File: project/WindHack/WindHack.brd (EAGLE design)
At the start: 79 x 43.7 mm, 48 parts, among them SW1 SSSS810701, SW2 SSSS810701, U1 LazuriteBLE, U10 BK-913, U2 BM1383AGLV, U3 KXG03, U4 BM1422AGMV, U5 DF40C-20DS-0.4V, U6 BHXXPB1WFV, U7 MOLEX-SD-503398-1892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

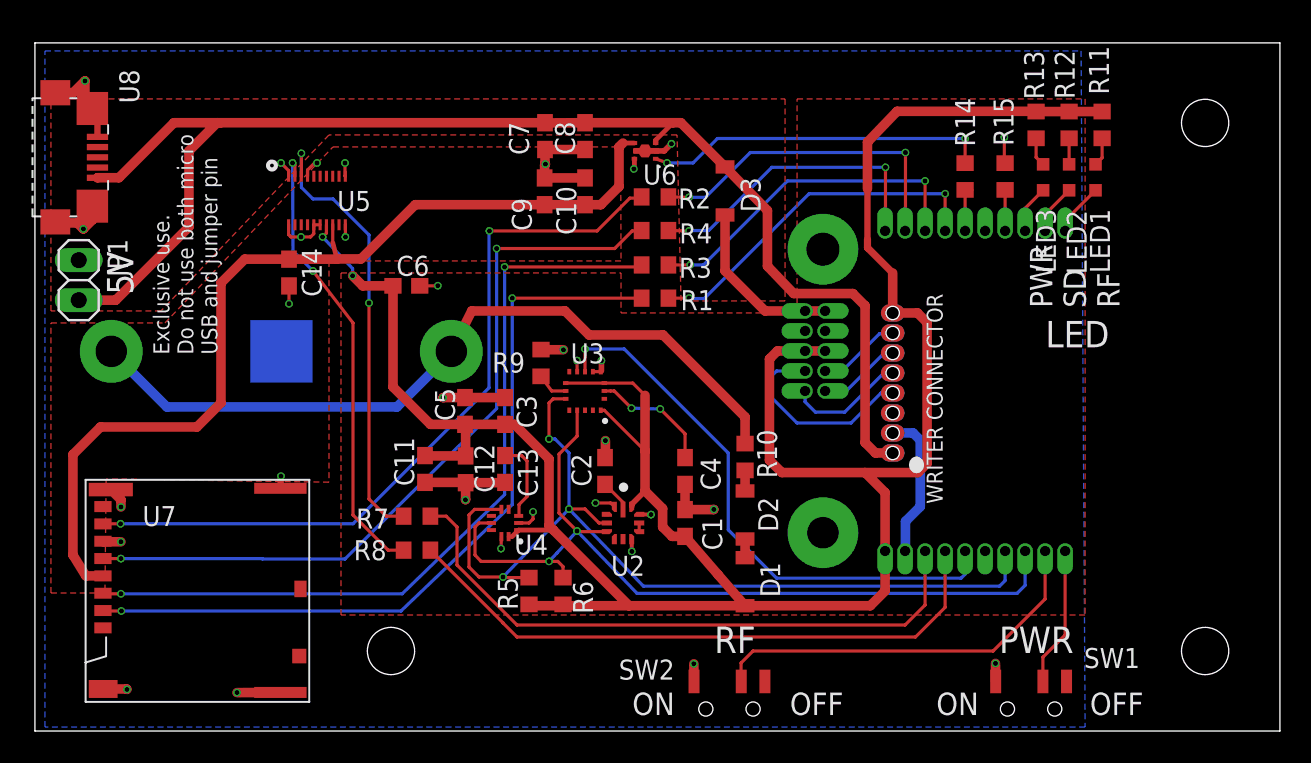
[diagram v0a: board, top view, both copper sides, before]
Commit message: modified to rev1A
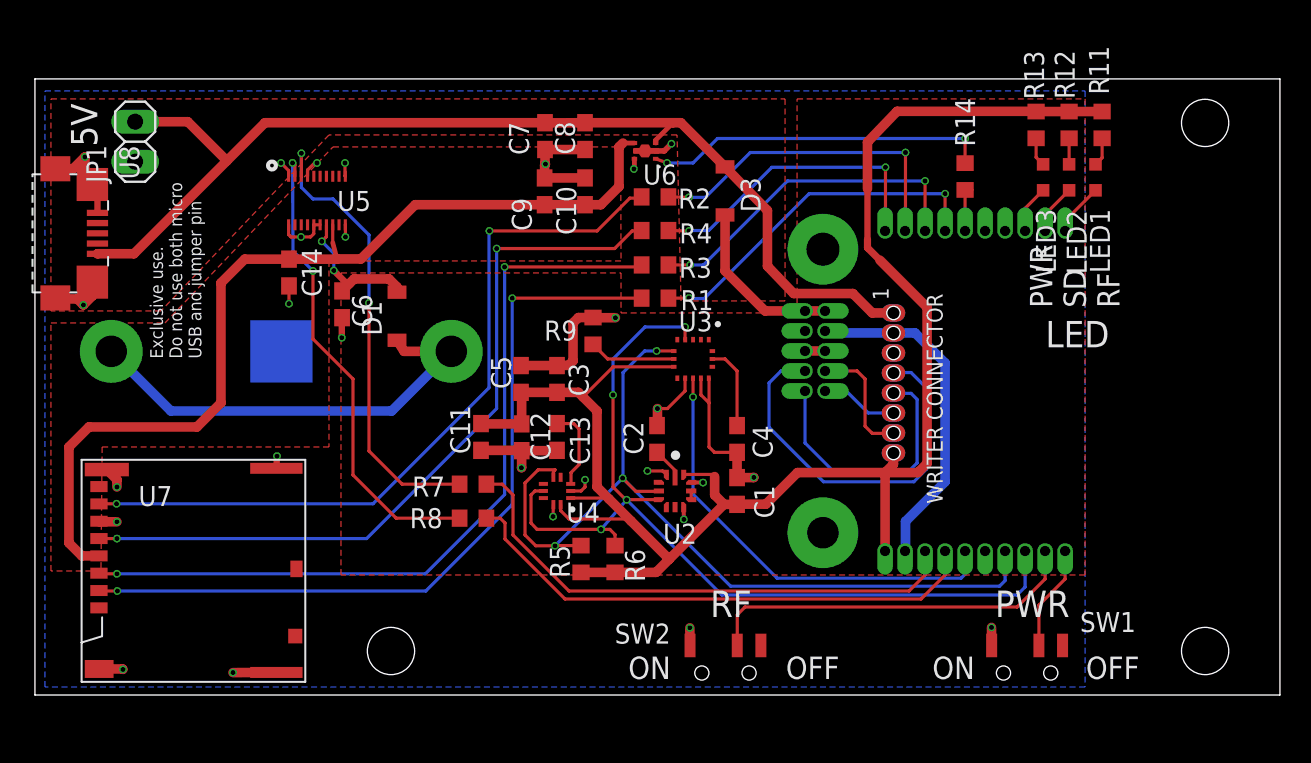
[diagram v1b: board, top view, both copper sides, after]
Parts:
- removed D2: RF071MM2S, lz-shield:RF071MM2S
- removed R10: 100, rcl:R0603
- removed R15: 0, rcl:R0603
- C6: value 0.1uF -> 1uF
- moved D1 27.8 mm to (35.1, 28.9), turned to 0 degrees
- moved JP1 9.49 mm to (18.4, 40.0), turned to 90 degrees
- moved U3 7.15 mm to (53.8, 26.2)
- moved U8 4.83 mm to (13.4, 34.1)
- moved C6 4.24 mm to (31.6, 29.6), turned to 270 degrees
- moved C11 4.10 mm to (40.4, 21.2)
- moved C12 4.10 mm to (43.0, 21.2)
- moved C5 4.10 mm to (42.9, 24.9)
- moved R8 4.10 mm to (39.9, 16.1)
- moved R7 4.10 mm to (39.9, 18.2)
- moved U4 3.88 mm to (45.2, 17.8)
- moved C13 3.88 mm to (45.2, 21.2)
- moved C3 3.88 mm to (45.2, 24.9)
- moved C1 3.88 mm to (56.6, 17.8)
- moved U2 3.88 mm to (52.7, 17.8)
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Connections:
- net ACCEL_INT renamed GYRO_INT
- net BT_SW renamed RF_SW
- removed net +2.4V_RSV: R10.2, U10.VDD1, U10.VDD2
- removed net GPS_PRS: R15.2, U1.7
- removed net N$9: D2.C, R10.1
- new net +3V_RSV: C6.1, D1.A, U5.14
- net +3V3: no longer C6.1, D1.A, U5.14
- net GND: no longer R15.1
- net N$8: now also U10.VDD1, U10.VDD2; no longer D2.A
- net TEST0: now also U$1.7_1; no longer U$1.7_2
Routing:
- net +3V3: track 161.7 -> 110.8 mm, vias 2 -> 0
- net +2.4V_RSV: track 49.4 -> 0.00 mm
- net N$8: track 1.19 -> 28.6 mm
- net GND: track 72.6 -> 94.6 mm, vias 32 -> 28
- net +5V: track 85.9 -> 69.7 mm
- net TEST1N: track 12.8 -> 24.9 mm
- net 1: track 7.55 -> 17.1 mm
- net +3V_RSV: track 0.00 -> 9.03 mm, vias 0 -> 2
- net GYRO_INT: track 36.0 -> 28.4 mm
- net SERIAL2_RX: track 39.6 -> 34.1 mm
- net SERIAL2_TX: track 39.4 -> 34.1 mm
- net SCL: track 55.2 -> 59.4 mm, vias 2 -> 4
- net N$5: track 2.04 -> 5.51 mm
- net GPS_PRS: track 2.60 -> 0.00 mm
- net TEST0: track 5.29 -> 7.75 mm
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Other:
- board size 79 x 43.7 mm -> 79 x 39.1 mm
- board text added: "1"
- board text added: "WindHack rev1A"
- board text removed: "WindHack rev1"
- board text removed: "●"

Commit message: updated to rev 1A'
- moved C6/C4/D1 location
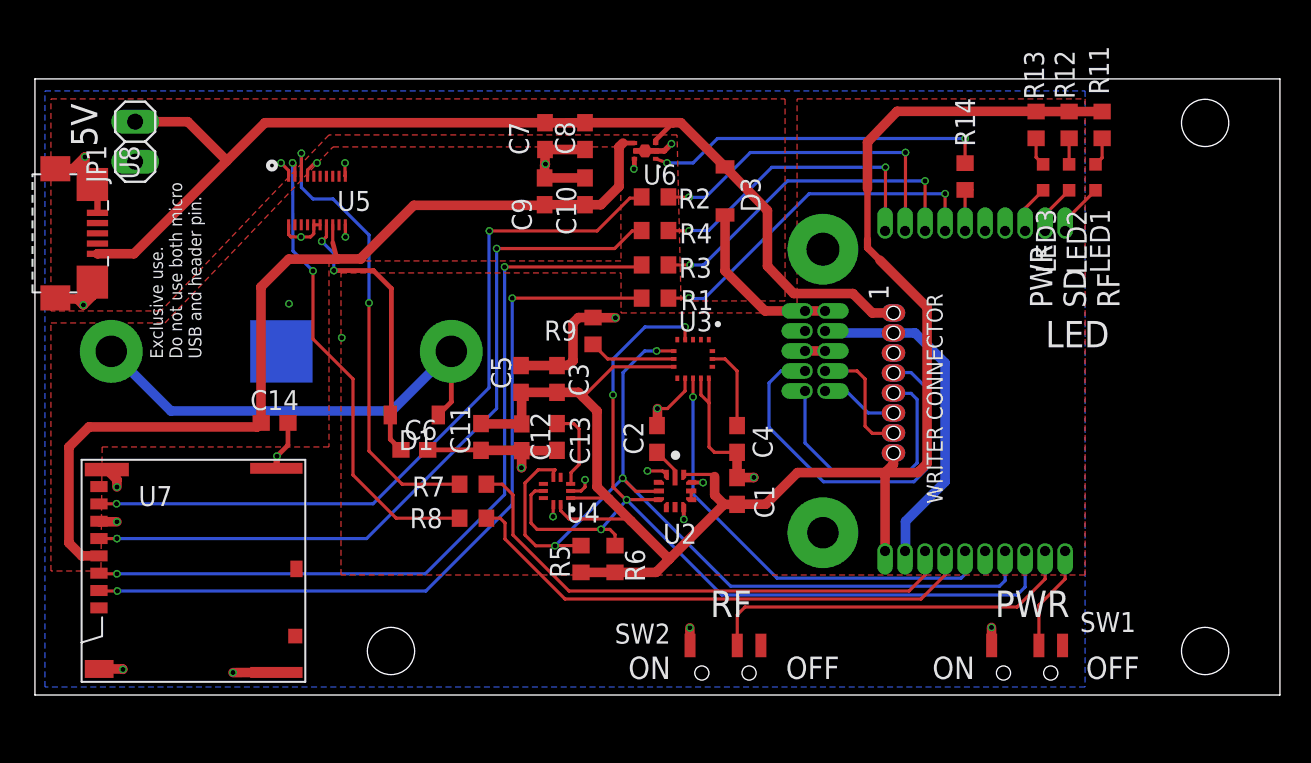
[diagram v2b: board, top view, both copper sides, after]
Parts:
- moved C6 10.3 mm to (36.2, 20.4), turned to 0 degrees
- moved C14 9.59 mm to (27.3, 22.1), turned to 0 degrees
- moved D1 6.36 mm to (36.1, 22.6), turned to 90 degrees
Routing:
- net +3V_RSV: track 9.03 -> 18.0 mm
- net GND: track 94.6 -> 98.0 mm
- net LDO3V: track 60.4 -> 61.0 mm
- net N$8: track 28.6 -> 29.1 mm
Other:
- board text added: "Exclusive use. Do not use both micro USB and header pin."
- board text removed: "Exclusive use. Do not use both micro USB and jumper pin"

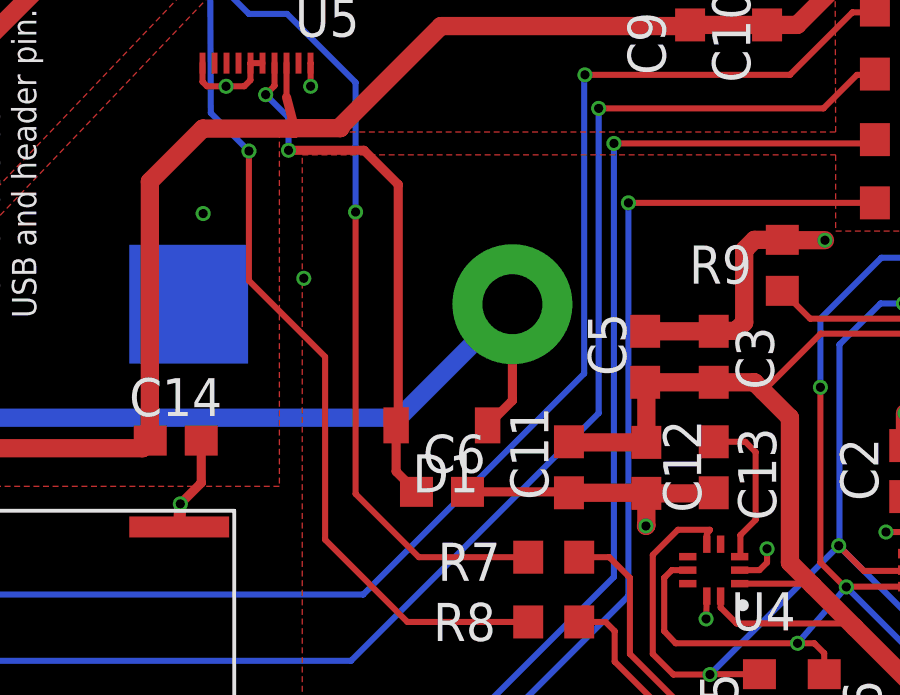
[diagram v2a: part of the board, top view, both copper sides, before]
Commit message: update WindHack and lz-shield(RF071MM2S)
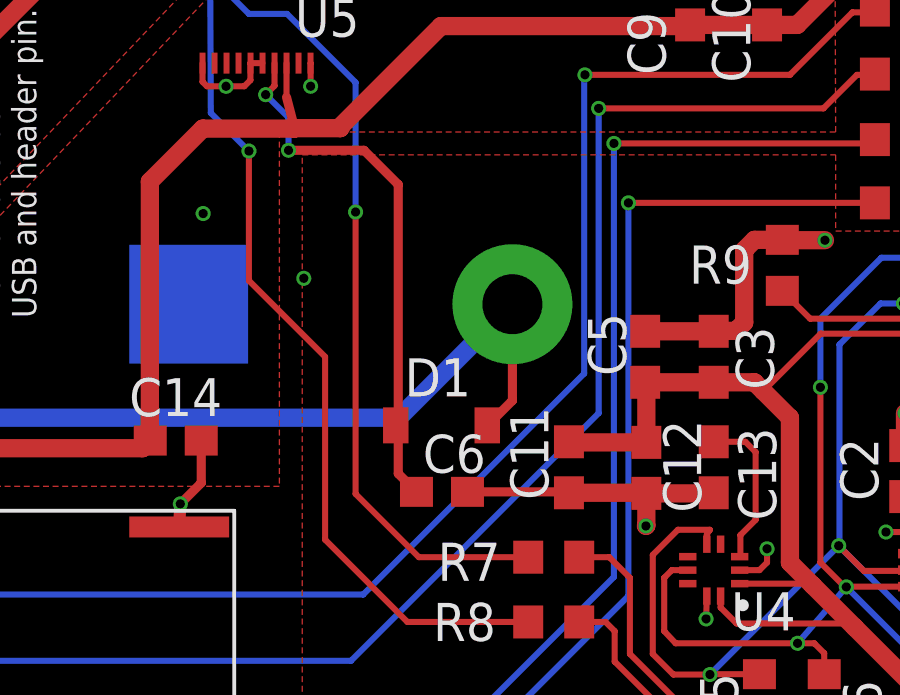
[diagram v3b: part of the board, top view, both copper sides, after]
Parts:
- turned D1 to 270 degrees
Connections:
- net +3V_RSV: now also D1.C; no longer D1.A
- net N$8: now also D1.A; no longer D1.C
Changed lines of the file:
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@@
 <layers>
 <layer number="1" name="Top" color="4" fill="1" visible="yes" active="yes"/>
-<layer number="16" name="Bottom" color="1" fill="1" visible="yes" active="yes"/>
+<layer number="16" name="Bottom" color="1" fill="1" visible="no" active="yes"/>
 <layer number="17" name="Pads" color="2" fill="1" visible="yes" active="yes"/>
 <layer number="18" name="Vias" color="2" fill="1" visible="yes" active="yes"/>
 <layer number="19" name="Unrouted" color="6" fill="1" visible="yes" active="yes"/>
 <layer number="20" name="Dimension" color="15" fill="1" visible="yes" active="yes"/>
-<layer number="21" name="tPlace" color="7" fill="1" visible="yes" active="yes"/>
-<layer number="22" name="bPlace" color="7" fill="1" visible="yes" active="yes"/>
+<layer number="21" name="tPlace" color="7" fill="1" visible="no" active="yes"/>
+<layer number="22" name="bPlace" color="7" fill="1" visible="no" active="yes"/>
 <layer number="23" name="tOrigins" color="15" fill="1" visible="no" active="yes"/>
 <layer number="24" name="bOrigins" color="15" fill="1" visible="no" active="yes"/>
-<layer number="25" name="tNames" color="7" fill="1" visible="no" active="yes"/>
+<layer number="25" name="tNames" color="7" fill="1" visible="yes" active="yes"/>
 <layer number="26" name="bNames" color="7" fill="1" visible="no" active="yes"/>
 <layer number="27" name="tValues" color="7" fill="1" visible="no" active="yes"/>
@@
 <layer number="37" name="tTest" color="7" fill="1" visible="no" active="yes"/>
 <layer number="38" name="bTest" color="7" fill="1" visible="no" active="yes"/>
-<layer number="39" name="tKeepout" color="4" fill="11" visible="no" active="yes"/>
+<layer number="39" name="tKeepout" color="4" fill="11" visible="yes" active="yes"/>
 <layer number="40" name="bKeepout" color="1" fill="11" visible="no" active="yes"/>
-<layer number="41" name="tRestrict" color="4" fill="10" visible="no" active="yes"/>
+<layer number="41" name="tRestrict" color="4" fill="10" visible="yes" active="yes"/>
 <layer number="42" name="bRestrict" color="1" fill="10" visible="no" active="yes"/>
 <layer number="43" name="vRestrict" color="2" fill="10" visible="no" active="yes"/>
-<layer number="44" name="Drills" color="7" fill="1" visible="no" active="yes"/>
-<layer number="45" name="Holes" color="7" fill="1" visible="no" active="yes"/>
+<layer number="44" name="Drills" color="7" fill="1" visible="yes" active="yes"/>
+<layer number="45" name="Holes" color="7" fill="1" visible="yes" active="yes"/>
 <layer number="46" name="Milling" color="3" fill="1" visible="no" active="yes"/>
-<layer number="47" name="Measures" color="7" fill="1" visible="no" active="yes"/>
+<layer number="47" name="Measures" color="7" fill="1" visible="yes" active="yes"/>
 <layer number="48" name="Document" color="7" fill="1" visible="yes" active="yes"/>
 <layer number="49" name="Reference" color="7" fill="1" visible="yes" active="yes"/>
 <layer number="50" name="dxf" color="7" fill="1" visible="no" active="no"/>
 <layer number="51" name="tDocu" color="7" fill="1" visible="yes" active="yes"/>
-<layer number="52" name="bDocu" color="7" fill="1" visible="yes" active="yes"/>
+<layer number="52" name="bDocu" color="7" fill="1" visible="no" active="yes"/>
 <layer number="53" name="tGND_GNDA" color="7" fill="9" visible="no" active="no"/>
 <layer number="54" name="bGND_GNDA" color="1" fill="9" visible="no" active="no"/>
@@
 <attribute name="VALUE" x="58.42" y="34.29" size="1.27" layer="27" rot="R90"/>
 </element>
-<element name="D1" library="lz-shield" package="RF071MM2S" value="RF071MM2S" x="36.15" y="22.606" smashed="yes" rot="R90">
-<attribute name="NAME" x="35.1732" y="20.3708" size="1.27" layer="25"/>
-<attribute name="VALUE" x="38.69" y="25.146" size="1.27" layer="27" rot="R180"/>
+<element name="D1" library="lz-shield" package="RF071MM2S" value="RF071MM2S" x="36.1384" y="22.606" smashed="yes" rot="R270">
+<attribute name="NAME" x="37.1152" y="24.8412" size="1.27" layer="25" rot="R180"/>
+<attribute name="VALUE" x="33.5984" y="20.066" size="1.27" layer="27"/>
 </element>
 <element name="U4" library="lz-shield" package="BM1422AGMV" value="BM1422AGMV" x="45.212" y="17.78" smashed="yes" rot="R270">
@@
 </signal>
 <signal name="+3V_RSV">
-<contactref element="D1" pad="A"/>
 <contactref element="U5" pad="14"/>
 <contactref element="C6" pad="1"/>
@@
 <wire x1="30.2768" y1="33.6296" x2="31.0388" y2="32.8676" width="0.2032" layer="16"/>
 <wire x1="31.0388" y1="32.8676" x2="31.0388" y2="31.7754" width="0.2032" layer="16"/>
-<wire x1="35.3036" y1="20.3898" x2="34.625" y2="21.0684" width="0.3048" layer="1"/>
-<wire x1="34.625" y1="21.0684" x2="34.625" y2="22.606" width="0.3048" layer="1"/>
 <wire x1="31.0388" y1="31.7754" x2="33.5534" y2="31.7754" width="0.3048" layer="1"/>
 <wire x1="33.5534" y1="31.7754" x2="34.6964" y2="30.6324" width="0.3048" layer="1"/>
-<wire x1="34.6964" y1="30.6324" x2="34.6964" y2="22.6774" width="0.3048" layer="1"/>
-<wire x1="34.6964" y1="22.6774" x2="34.625" y2="22.606" width="0.3048" layer="1"/>
+<wire x1="34.6964" y1="30.6324" x2="34.6964" y2="22.606" width="0.3048" layer="1"/>
+<wire x1="34.6964" y1="22.606" x2="34.6964" y2="20.997" width="0.3048" layer="1"/>
+<wire x1="34.6964" y1="20.997" x2="35.3036" y2="20.3898" width="0.3048" layer="1"/>
+<contactref element="D1" pad="C"/>
+<wire x1="34.6134" y1="22.606" x2="34.6964" y2="22.606" width="0.3048" layer="1"/>
 </signal>
 <signal name="RF_SW">
@@
 <contactref element="U10" pad="VDD2"/>
 <contactref element="U10" pad="VDD1"/>
-<contactref element="D1" pad="C"/>
 <wire x1="16.9114" y1="26.6446" x2="20.696" y2="22.86" width="0.6096" layer="16"/>
 <wire x1="20.696" y1="22.86" x2="34.7168" y2="22.86" width="0.6096" layer="16"/>
 <wire x1="38.5014" y1="26.6446" x2="34.7168" y2="22.86" width="0.6096" layer="16"/>
 <wire x1="38.5014" y1="26.6446" x2="38.5014" y2="23.4324" width="0.3048" layer="1"/>
-<wire x1="38.5014" y1="23.4324" x2="37.675" y2="22.606" width="0.3048" layer="1"/>
+<contactref element="D1" pad="A"/>
+<wire x1="37.6634" y1="22.606" x2="37.675" y2="22.606" width="0.2032" layer="1"/>
+<wire x1="37.675" y1="22.606" x2="38.5014" y2="23.4324" width="0.3048" layer="1"/>
 </signal>
 </signals>
